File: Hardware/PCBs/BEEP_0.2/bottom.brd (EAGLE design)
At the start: 85 x 73 mm, 60 parts, among them IC1 74HCT00D, Q1 DMN2075U, Q2 IRLML2244, Q5 IRLML2244, Q6 IRLML2244, Q8 IRLML2244, U1 LM239AMDREP, U2 ATTINY10-TSHR

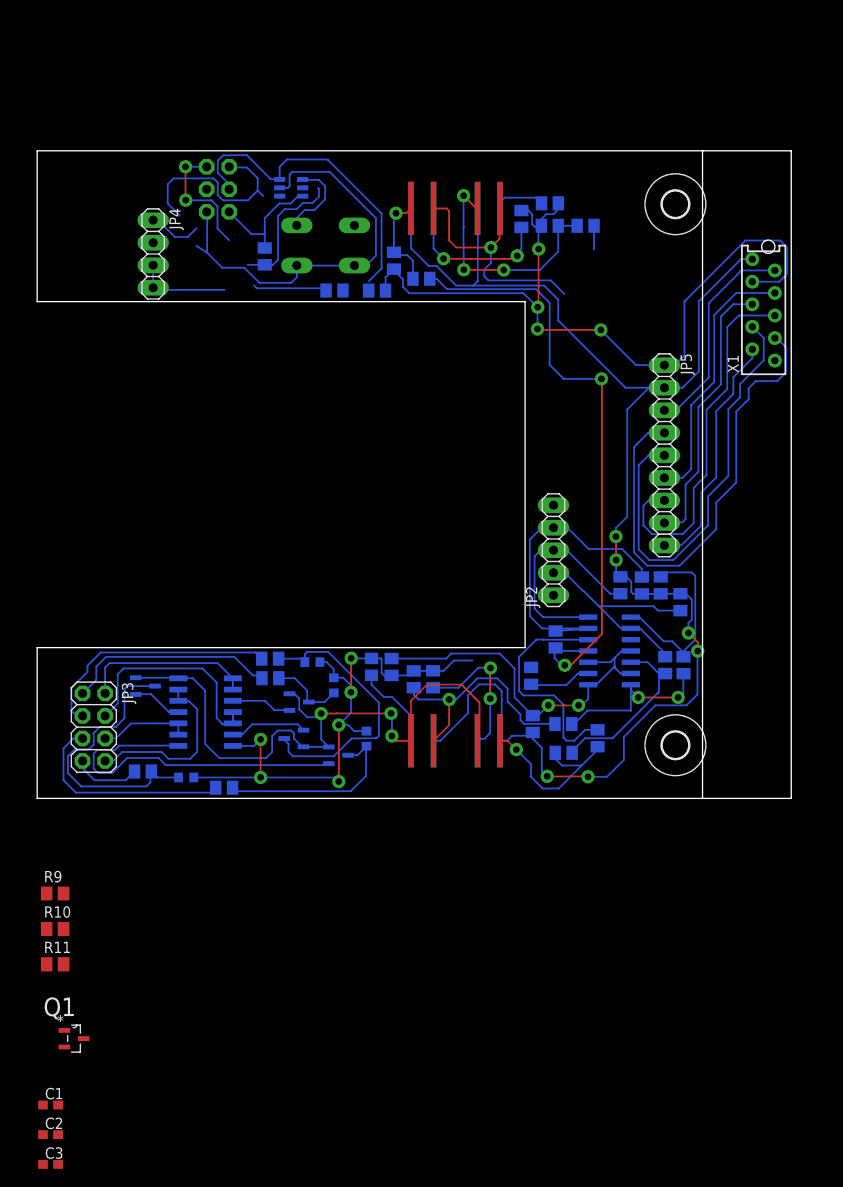
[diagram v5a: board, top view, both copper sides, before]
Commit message: continue work on bottom pcb add simulation for attiny on/off
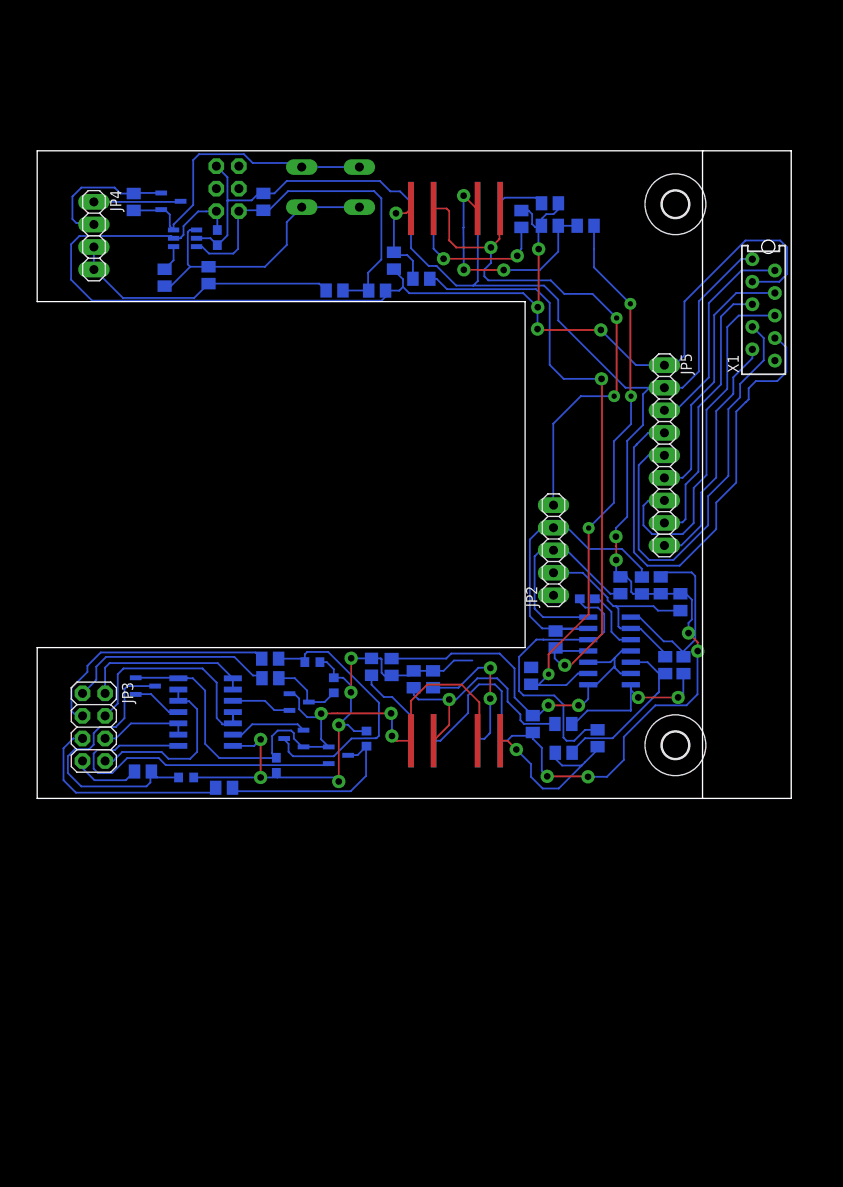
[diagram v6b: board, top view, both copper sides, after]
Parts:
- R9: value 10k -> 1k
- moved C1 99.6 mm to (20.4, 63.2), flipped to the bottom, turned to 90 degrees
- moved Q1 95.0 mm to (15.2, 67.3), flipped to the bottom, turned to 180 degrees
- moved C3 87.9 mm to (62.1, 22.5), flipped to the bottom
- moved R11 86.4 mm to (11.0, 67.2), flipped to the bottom, turned to 270 degrees
- moved R10 75.7 mm to (19.4, 59.0), flipped to the bottom, turned to 270 degrees
- moved R9 70.5 mm to (14.5, 58.7), flipped to the bottom, turned to 270 degrees
- moved C2 48.8 mm to (27.1, 3.73), flipped to the bottom, turned to 270 degrees
- moved U2 13.2 mm to (16.8, 63.1)
- moved JP4 6.99 mm to (6.48, 63.4)
- moved S1 6.60 mm to (33.2, 68.9), turned to 0 degrees
- moved R36 6.15 mm to (25.6, 67.2), turned to 90 degrees
- moved JP1 1.09 mm to (21.6, 68.7)
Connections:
- removed net TINY_VCC: JP1.2
- net +3V3: now also C3.1, JP1.2; no longer R10.2
- net +5V: now also C2.1
- net +7V: now also R10.2
- net BATT_GND: no longer JP1.6
- net GND: now also C2.2, C3.2, JP1.6
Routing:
- net N$47: track 9.64 -> 64.9 mm, vias 0 -> 4
- net GND: track 199.8 -> 248.1 mm
- net +5V: track 103.0 -> 137.3 mm, vias 4 -> 6
- net RESET: track 13.7 -> 40.8 mm
- net +3V3: track 182.9 -> 209.2 mm
- net PB2/SOFT_OFF: track 8.40 -> 32.3 mm
- net TPIDATA: track 22.8 -> 0.00 mm
- net TINY_VCC: track 14.4 -> 0.00 mm, vias 2 -> 0
- net TPICLK: track 12.1 -> 0.00 mm
- net +7V: track 19.1 -> 31.0 mm
- net PB1/TPICLK: track 24.0 -> 34.7 mm
- net BATT_GND: track 26.3 -> 15.9 mm
- net SWITCHED_GND: track 6.08 -> 9.80 mm
- net PB0/TPIDATA: track 0.00 -> 2.97 mm
- net ENC_L2: track 26.1 -> 25.6 mm

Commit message: add modified gcode export script finish bottom pcb add gcode for cnc
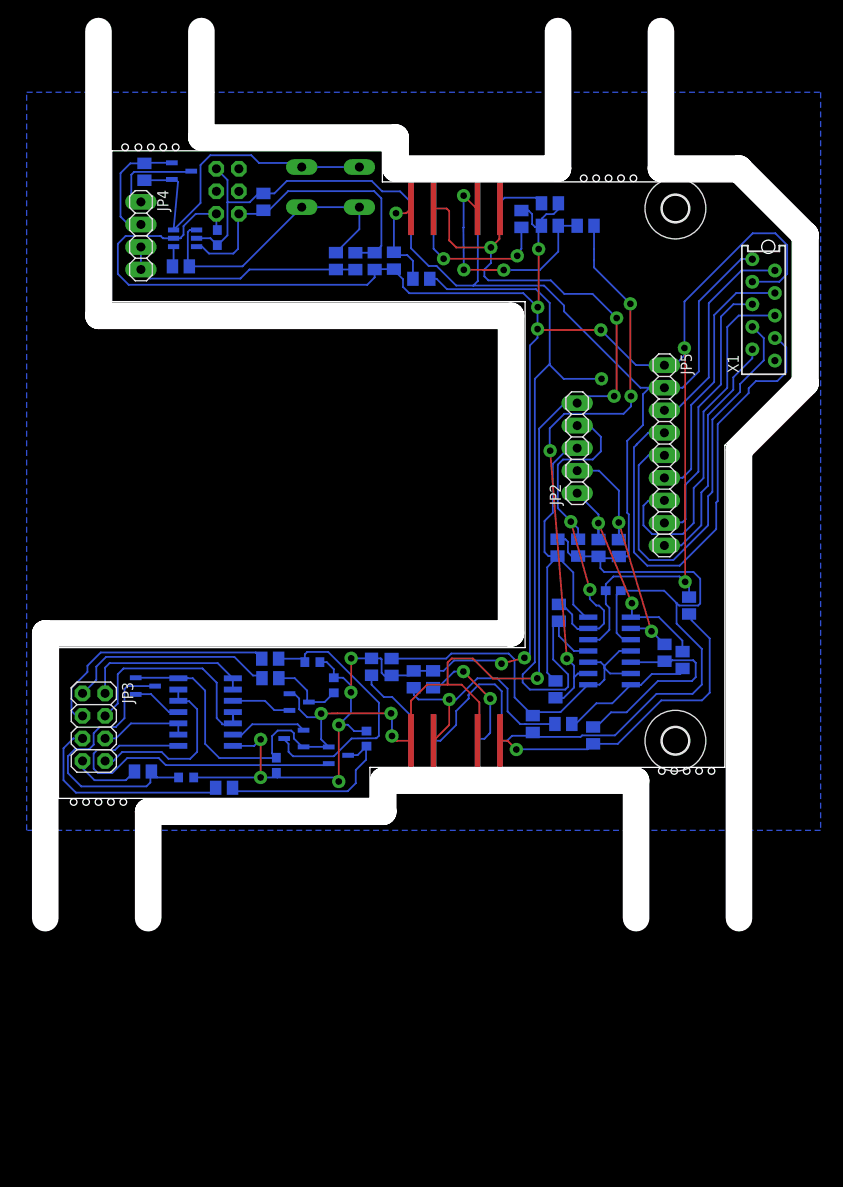
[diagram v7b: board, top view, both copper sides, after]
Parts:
- moved R15 18.2 mm to (73.6, 21.7)
- moved R10 14.4 mm to (33.8, 60.6)
- moved JP2 11.8 mm to (61.0, 39.5)
- moved R21 9.24 mm to (65.7, 28.2), turned to 270 degrees
- moved R23 8.36 mm to (61.1, 28.3)
- moved R22 8.26 mm to (58.7, 28.3)
- moved R20 8.18 mm to (63.4, 28.2)
- moved JP4 5.30 mm to (11.8, 63.4)
- moved R35 4.06 mm to (36.0, 60.6), turned to 270 degrees
- moved R27 3.85 mm to (62.8, 7.10), turned to 270 degrees
- moved Q1 3.61 mm to (16.4, 70.7)
- moved R11 3.61 mm to (12.2, 70.6)
- moved R34 3.34 mm to (38.1, 60.6), turned to 90 degrees
- moved R32 3.14 mm to (58.5, 12.3)
- moved C3 3.06 mm to (65.0, 23.4)
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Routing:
- net GND: track 248.1 -> 293.2 mm, vias 10 -> 14
- net +5V: track 137.3 -> 171.9 mm, vias 6 -> 7
- net N$49: track 69.1 -> 85.3 mm, vias 2 -> 1
- net ENC_L2_RAW: track 20.7 -> 36.5 mm
- net ENC_R1: track 24.8 -> 39.0 mm
- net +3V3: track 209.2 -> 222.5 mm, vias 6 -> 0
- net ENC_L1: track 21.5 -> 27.6 mm, vias 0 -> 2
- net RESET: track 40.8 -> 35.3 mm
- net ENC_L2: track 25.6 -> 30.4 mm, vias 0 -> 2
- net N$44: track 20.1 -> 15.3 mm, vias 2 -> 0
- net N$45: track 19.2 -> 23.2 mm
- net ENC_R2: track 35.7 -> 39.4 mm, vias 0 -> 2
- net +7V: track 31.0 -> 27.6 mm
- net N$46: track 16.5 -> 14.1 mm
- net PB1/TPICLK: track 34.7 -> 36.9 mm
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- added copper zone on layer 16, net GND
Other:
- board size 85 x 73 mm -> 85.7 x 100 mm

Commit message: minor pcb changes
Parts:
- C1: value (none) -> 100n
- moved C1 0.50 mm to (20.9, 63.2)
- moved C2 0.50 mm to (27.6, 3.73)
- moved C3 0.50 mm to (65.5, 23.4)
- moved D1 0.50 mm to (44.0, 3.50)
- moved D2 0.50 mm to (51.5, 3.50)
- moved D3 0.50 mm to (51.5, 69.5)
- moved D4 0.50 mm to (44.0, 69.5)
- moved IC1 0.50 mm to (19.6, 9.73)
- moved JP1 0.50 mm to (22.1, 68.4)
- moved JP2 0.50 mm to (61.5, 39.5)
- moved JP3 0.50 mm to (6.98, 8.03)
- moved JP4 0.50 mm to (12.3, 63.4)
- moved JP5 0.50 mm to (71.3, 38.7)
- moved Q1 0.50 mm to (16.9, 70.7)
- moved Q2 0.50 mm to (29.5, 6.75)
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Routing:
- net PB1/TPICLK: track 36.9 -> 34.2 mm
- net PWM_OUT2: track 27.2 -> 27.9 mm
